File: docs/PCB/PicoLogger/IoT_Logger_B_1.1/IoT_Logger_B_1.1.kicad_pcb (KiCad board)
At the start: 2 copper layers, 94.7 x 71.8 mm, 147 parts, among them J1 JTAG, J2 ESP_UART, J3 USB-C, J4 Sensor, J5 LCD 16x2, J6 Additional, J7 SPI, J8 CON, J9 CAN, Q1 BSS138, Q2 AO3407, Q3 BC817-40-DIO, Q4 BSS138, SW1 Tact Switch 6x6mm / 13mm, SW2 Tact Switch 6x6mm / 13mm, SW3 Tact Switch 6x6mm / 13mm, SW4 Tact Switch 6x6mm / 13mm, U1 STM32F412RGTx, U2 ESP32-C6-WROOM-1U, U3 AP63200WU, U4 PCA9306DCUR, U5 SN65HVD230DR, U6 MCP7940N-xSN, U7 TPD2EUSB30, U8 FM24CL16B, U9 MX25L25673GM2I-08G, Y1 3225-25M-SR, Y2 32.768K-CFPX217, Y3 QT3CD-32.768KEZY-T

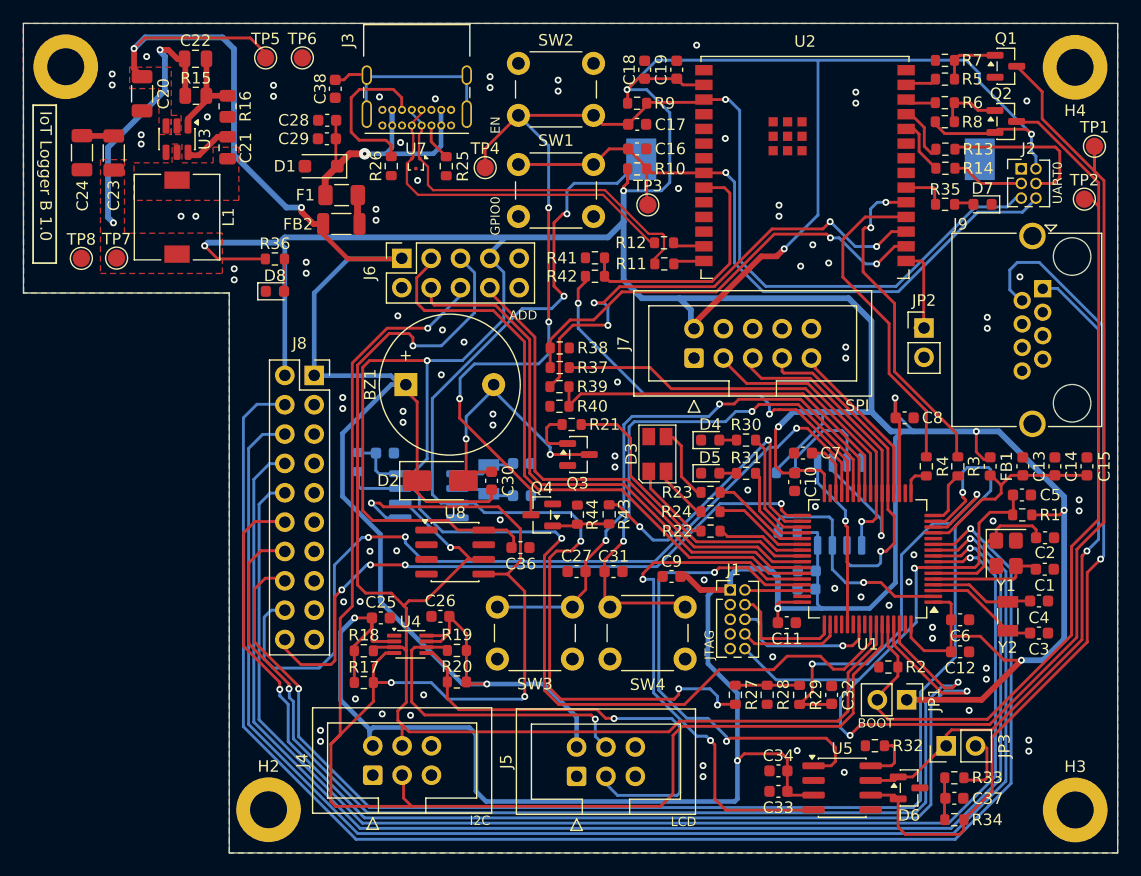
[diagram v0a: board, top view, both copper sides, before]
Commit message: New logger revisions added.
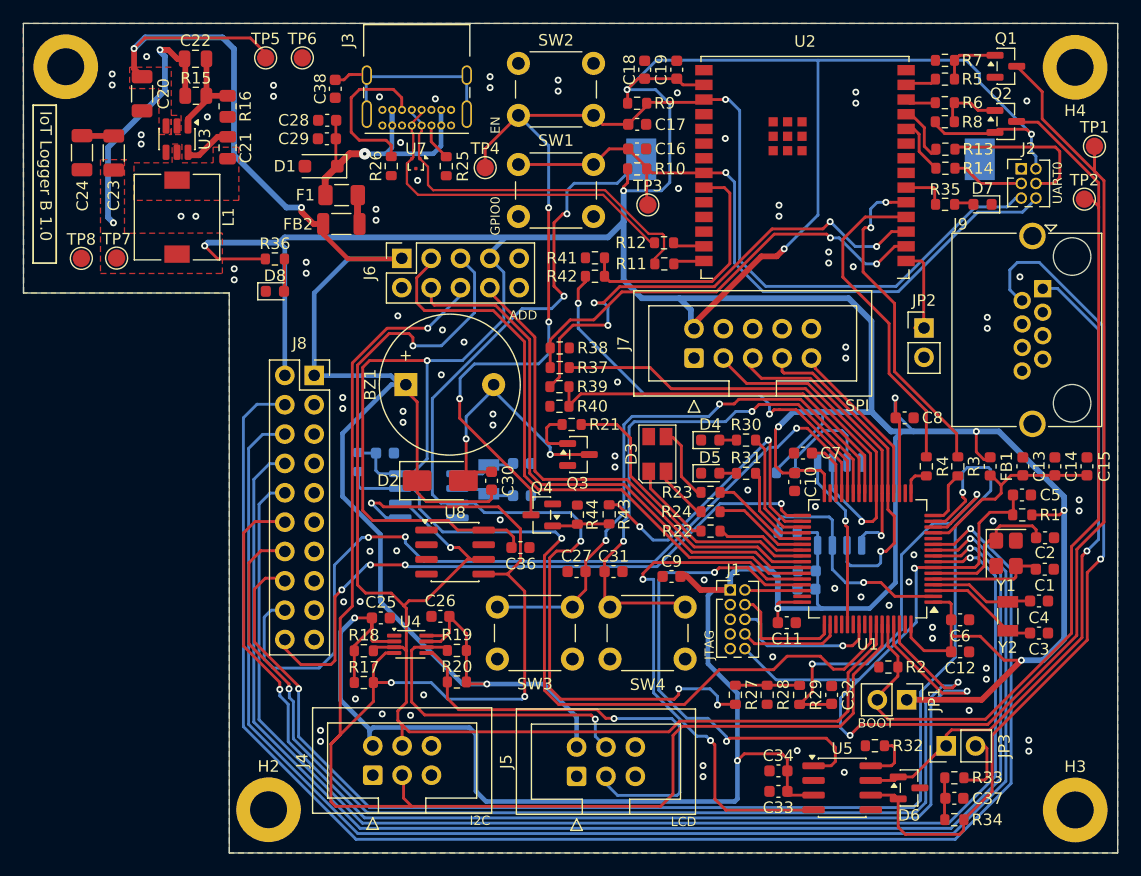
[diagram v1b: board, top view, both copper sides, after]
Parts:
- R1, R10, R2, R9: value 10kR -> 10k
- R17, R18: value 4k7R -> 4k7
- R19, R20, R45: value 4k7R -> 4K7
- R21: value 1kR -> 1K
- R25, R26: value 5k1R -> 5K1
- R27: value 200kR -> 200k
- R28: value 68kR -> 68k
- R43, R5, R6: value 1kR -> 1k
- R44, R7, R8: value 100kR -> 100k
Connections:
- U9 pad 2: SPI1_MISO -> SPI1_MOSI
- U9 pad 5: SPI1_MOSI -> SPI1_MISO
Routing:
- net SPI1_MISO: track 31.0 -> 25.6 mm
- net SPI1_MOSI: track 27.0 -> 30.4 mm
